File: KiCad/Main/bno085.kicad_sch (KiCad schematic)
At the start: 5 parts, among them J7 RJ45

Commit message: ok
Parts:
- C1000µF1: footprint (none) -> Capacitor_THT:CP_Radial_D17.0mm_P7.50mm
- J7: footprint (none) -> Connector_RJ:RJ45_Amphenol_54602-x08_Horizontal
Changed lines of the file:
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@@
 			)
 		)
-		(property "Footprint" ""
+		(property "Footprint" "Capacitor_THT:CP_Radial_D17.0mm_P7.50mm"
 			(at 98.7552 38.1 0)
 			(effects
@@
 			)
 		)
-		(property "Footprint" ""
+		(property "Footprint" "Connector_RJ:RJ45_Amphenol_54602-x08_Horizontal"
 			(at 72.39 53.975 90)
 			(effects

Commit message: ota webserver ok
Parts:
- added C1000µF3: C_Polarized, Capacitor_THT:CP_Radial_D17.0mm_P7.50mm, symbol Device:C_Polarized
- added J9: RJ45, Connector_RJ:RJ45_Amphenol_54602-x08_Horizontal, symbol Connector:RJ45
- added R7, R8, R9: 4.7K, symbol Device:R
- added U4: (no value), symbol gy-bno08x:gy-bno08x
- U3: value ~ -> (none)
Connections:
- new net: J9.6, R7.1, U4. (PS0)
- new net: C1000µF3.1, J9.1, J9.3, J9.8, R7.2, R8.2, R9.2, U4. (PS0)
- new net: J9.5, R8.1, U4. (PS0)
- new net: C1000µF3.2, J9.2, J9.4, J9.7, U4. (PS0)
- new net: R9.1, U4. (PS0)

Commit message: bno085 et moteurs OK
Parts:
- added C1000µF4: C_Polarized, Capacitor_THT:CP_Radial_D17.0mm_P7.50mm, symbol Device:C_Polarized
- added J10: RJ45, Connector_RJ:RJ45_Amphenol_54602-x08_Horizontal, symbol Connector:RJ45
- added J2: Conn_01x02_Pin, symbol Connector:Conn_01x02_Pin
- added R10, R11, R12: 4.7K, symbol Device:R
- added U7: (no value), symbol gy-bno08x:gy-bno08x
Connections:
- net at U4. (PS0): now also R9.1
- new net: J10.6, R11.1, U7. (PS0)
- new net: C1000µF4.1, J10.1, J10.8, J2.1 (Pin_1), R10.2, R11.2, R12.2, U7. (PS0)
- new net: C1000µF4.2, J10.2, J10.7, J2.2 (Pin_2), U7. (PS0)
- new net: J10.3, U7. (PS0)
- new net: J10.4, U7. (PS0)
- new net: J10.5, R12.1, U7. (PS0)
- new net: R10.1, U7. (PS0)
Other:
- moved on the sheet: C1000µF1, C1000µF3, J7, J9, R3, R4, R7, R8, R9, U3, U4

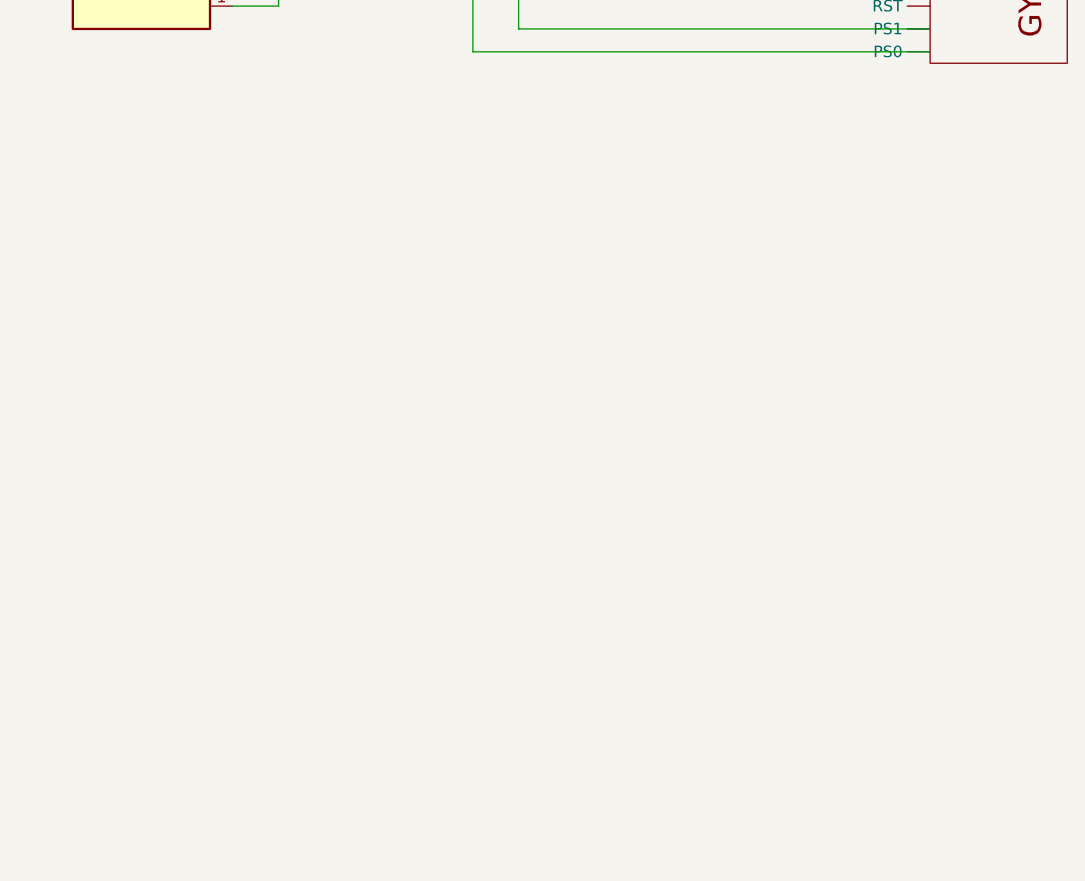
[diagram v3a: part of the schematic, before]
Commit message: restructuration du repository
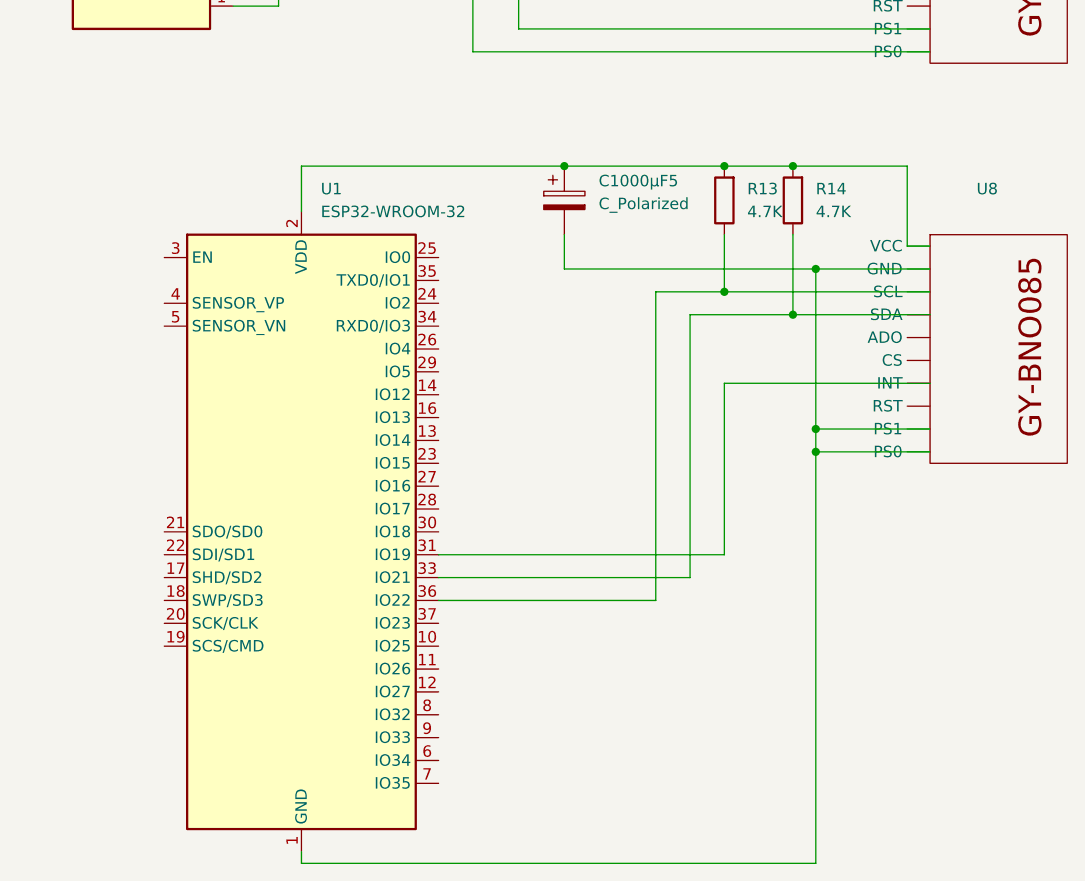
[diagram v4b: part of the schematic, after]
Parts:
- added C1000µF5: C_Polarized, Capacitor_THT:CP_Radial_D17.0mm_P7.50mm, symbol Device:C_Polarized
- added R13, R14: 4.7K, symbol Device:R
- added U1: ESP32-WROOM-32, RF_Module:ESP32-WROOM-32, symbol RF_Module:ESP32-WROOM-32
- added U8: (no value), symbol gy-bno08x:gy-bno08x
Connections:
- net at U4. (PS0): now also R9.1
- new net: R13.1, U1.36 (IO22), U8. (PS0)
- new net: C1000µF5.1, R13.2, R14.2, U1.2 (VDD), U8. (PS0)
- new net: C1000µF5.2, U1.1 (GND), U1.15 (GND), U1.38 (GND), U1.39 (GND), U8. (PS0)
- new net: U1.31 (IO19), U8. (PS0)
- new net: R14.1, U1.33 (IO21), U8. (PS0)

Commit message: ok
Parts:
- added J4: Conn_01x02_Pin, symbol Connector:Conn_01x02_Pin
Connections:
- net at C1000µF5.1, R13.2, R14.2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: now also J4.2 (Pin_2)
- net at U4. (PS0): now also R9.1
- net at C1000µF5.2, U1.1 (GND), U1.15 (GND)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: now also J4.1 (Pin_1)
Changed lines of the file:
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@@
+	)
+	(junction
+		(at 191.77 151.13)
+		(diameter 0)
+		(color 0 0 0 0)
 	)
 	(junction
@@
 	)
 	(junction
+		(at 191.77 73.66)
+		(diameter 0)
+		(color 0 0 0 0)
+	)
+	(junction
 		(at 199.39 19.05)
 		(diameter 0)
@@
 	(wire
 		(pts
+			(xy 250.19 130.81) (xy 191.77 130.81)
+		)
+		(stroke
+			(width 0)
+			(type default)
+		)
+	)
+	(wire
+		(pts
 			(xy 50.8 20.32) (xy 50.8 25.4)
 		)
@@
 	(wire
 		(pts
+			(xy 191.77 73.66) (xy 199.39 73.66)
+		)
+		(stroke
+			(width 0)
+			(type default)
+		)
+	)
+	(wire
+		(pts
 			(xy 50.8 20.32) (xy 81.28 20.32)
 		)
@@
 	(wire
 		(pts
+			(xy 191.77 133.35) (xy 191.77 151.13)
+		)
+		(stroke
+			(width 0)
+			(type default)
+		)
+	)
+	(wire
+		(pts
 			(xy 44.45 82.55) (xy 44.45 101.6)
 		)
@@
 	(wire
 		(pts
+			(xy 250.19 133.35) (xy 191.77 133.35)
+		)
+		(stroke
+			(width 0)
+			(type default)
+		)
+	)
+	(wire
+		(pts
 			(xy 199.39 50.8) (xy 240.03 50.8)
 		)
@@
 	(wire
 		(pts
-			(xy 170.18 73.66) (xy 199.39 73.66)
+			(xy 170.18 73.66) (xy 191.77 73.66)
 		)
 		(stroke
@@
 	(wire
 		(pts
-			(xy 170.18 151.13) (xy 227.33 151.13)
+			(xy 170.18 151.13) (xy 191.77 151.13)
 		)
 		(stroke
@@
 	(wire
 		(pts
+			(xy 191.77 151.13) (xy 227.33 151.13)
+		)
+		(stroke
+			(width 0)
+			(type default)
+		)
+	)
+	(wire
+		(pts
 			(xy 189.23 60.96) (xy 189.23 40.64)
 		)
@@
 	(wire
 		(pts
+			(xy 191.77 130.81) (xy 191.77 73.66)
+		)
+		(stroke
+			(width 0)
+			(type default)
+		)
+	)
+	(wire
+		(pts
 			(xy 67.31 119.38) (xy 113.03 119.38)
 		)
@@
 		)
 	)
+	(symbol
+		(lib_id "Connector:Conn_01x02_Pin")
+		(at 255.27 133.35 180)
+		(unit 1)
+		(body_style 1)
+		(exclude_from_sim no)
+		(in_bom yes)
+		(on_board yes)
+		(in_pos_files yes)
+		(dnp no)
+		(fields_autoplaced yes)
+		(property "Reference" "J4"
+			(at 256.54 130.8099 0)
+			(show_name no)
+			(do_not_autoplace no)
+			(effects
+				(font
+					(size 1.27 1.27)
+				)
+				(justify right)
+			)
+		)
+		(property "Value" "Conn_01x02_Pin"
+			(at 256.54 133.3499 0)
+			(show_name no)
+			(do_not_autoplace no)
+			(effects
+				(font
+					(size 1.27 1.27)
+				)
+				(justify right)
+			)
+		)
+		(property "Footprint" ""
+			(at 255.27 133.35 0)
+			(hide yes)
+			(show_name no)
+			(do_not_autoplace no)
+			(effects
+				(font
+					(size 1.27 1.27)
+				)
+			)
+		)
+		(property "Datasheet" ""
+			(at 255.27 133.35 0)
+			(hide yes)
+			(show_name no)
+			(do_not_autoplace no)
+			(effects
+				(font
+					(size 1.27 1.27)
+				)
+			)
+		)
+		(property "Description" "Generic connector, single row, 01x02, script generated"
+			(at 255.27 133.35 0)
+			(hide yes)
+			(show_name no)
+			(do_not_autoplace no)
+			(effects
+				(font
+					(size 1.27 1.27)
+				)
+			)
+		)
+		(pin "1"
+		)
+		(pin "2"
+		)
+		(instances
+			(project "main"
+				(path "/71abecfb-cf01-4845-b5b4-89a1f610326d/19b04c30-ba1c-490f-96af-2011eb9b2294"
+					(reference "J4")
+					(unit 1)
+				)
+			)
+		)
+	)
